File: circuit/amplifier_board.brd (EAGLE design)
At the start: 160 x 100 mm, 17 parts

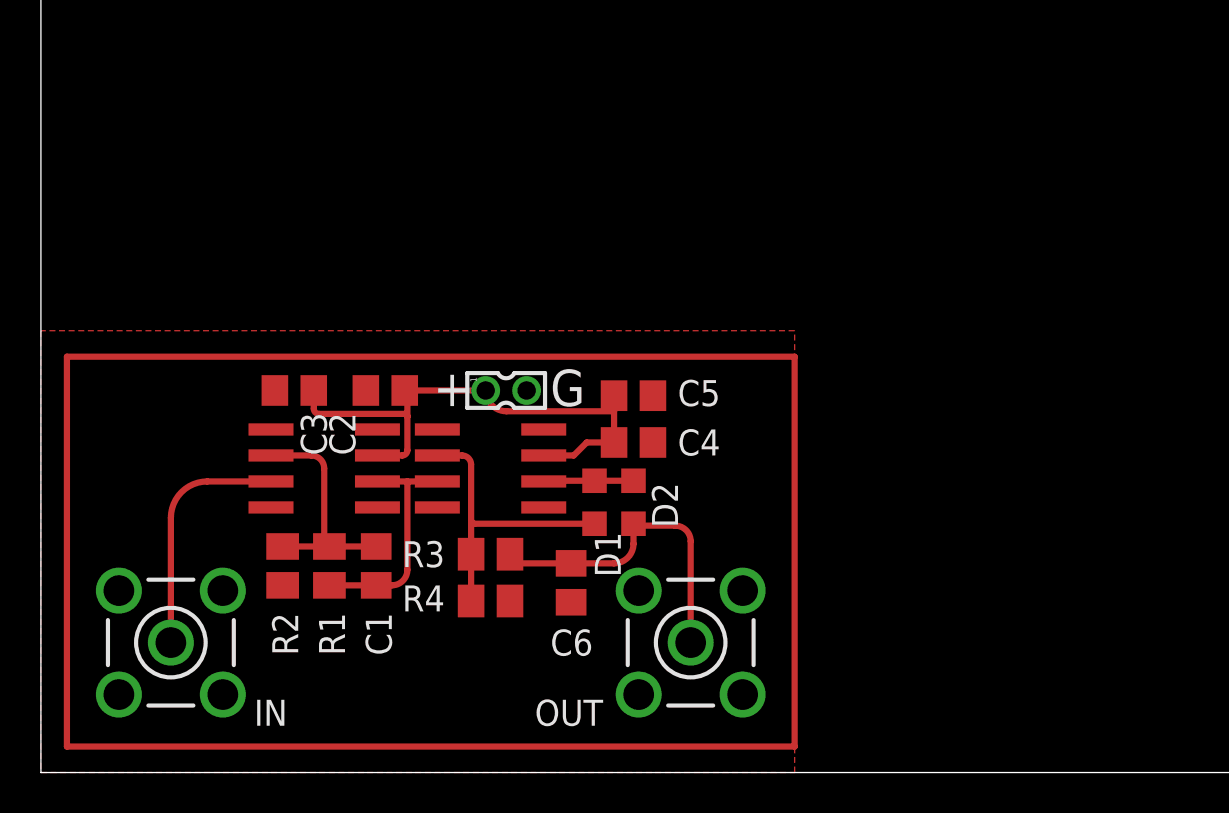
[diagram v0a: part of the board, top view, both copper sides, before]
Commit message: boards: Changed components to be correct; increased board size to be solderable.
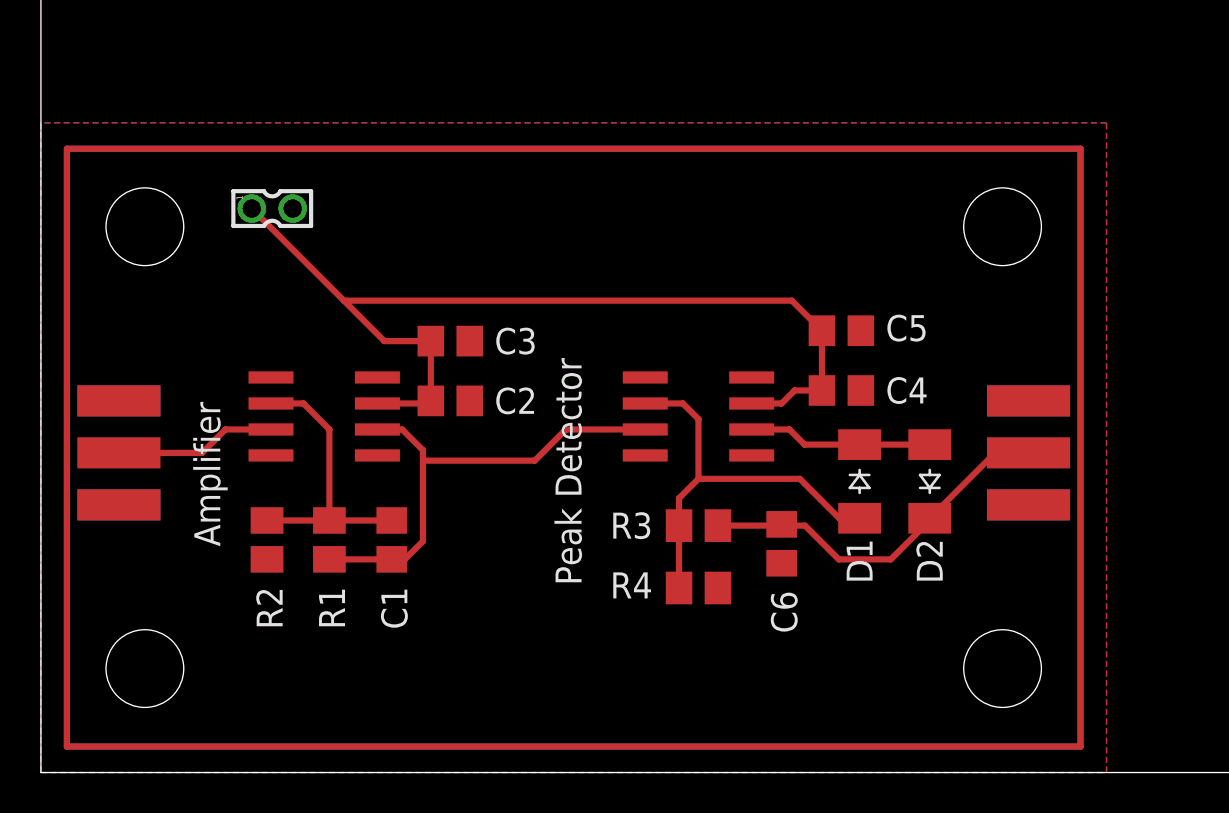
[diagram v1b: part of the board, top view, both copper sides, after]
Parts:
- C6: value 10uF -> 10nF
- D1, D2: value (none) -> MBR0540CT-ND; device 000phys605parts:SML0805 -> diode:SOD-123_MINI-SMA
- IN, OUT: value LTI-SASF54GT -> SMA_EDGE; device con-coax:LTI-SASF54GT -> SparkFun-Retired:SMA-EDGE
- MAX4104_1: value (none) -> Amplifier
- MAX4104_2: value (none) -> Peak Detector
- moved OUT 17.8 mm to (48.3, 13.1), turned to 90 degrees
- moved D2 14.5 mm to (43.4, 14.2)
- moved SUP 14.5 mm to (11.3, 27.6)
- moved D1 13.0 mm to (40.0, 14.2)
- moved C5 10.6 mm to (39.1, 21.6)
- moved C4 10.5 mm to (39.1, 18.7)
- moved MAX4104_2 10.5 mm to (32.1, 17.4)
- moved C6 10.5 mm to (36.2, 11.2)
- moved R3 10.3 mm to (32.1, 12.1)
- moved R4 10.2 mm to (32.1, 9.02)
- moved C3 7.99 mm to (20.0, 21.1), turned to 0 degrees
- moved IN 7.19 mm to (3.81, 13.1), turned to 90 degrees
- moved C2 3.22 mm to (20.0, 18.2), turned to 0 degrees
- moved MAX4104_1 2.54 mm to (13.8, 17.4)
- moved C1 1.48 mm to (17.1, 11.4)
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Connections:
- net DIG_READOUT: now also OUT.SIG; no longer OUT.1
- net GND: now also IN.GND@0, IN.GND@1, IN.GND@2, IN.GND@3, OUT.GND@0, OUT.GND@1, OUT.GND@2, OUT.GND@3; no longer IN.2, IN.3, IN.4, IN.5, OUT.2, OUT.3, OUT.4, OUT.5
- net IN: now also IN.SIG; no longer IN.1
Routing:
- net N$2: track 0.00 -> 157.5 mm
- net N$1: track 109.2 -> 157.5 mm
- net VCC: track 26.7 -> 47.6 mm
- net AMP: track 11.4 -> 23.5 mm
- net IN-_2: track 14.6 -> 20.2 mm
- net OUT_2: track 4.40 -> 9.06 mm
- net IN: track 11.7 -> 7.91 mm
- net IN-_1: track 11.2 -> 13.9 mm
- net DIG_READOUT: track 15.6 -> 18.1 mm
- added copper zone on layer 16, net GND
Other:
- board text removed: "+"
- board text removed: "G"

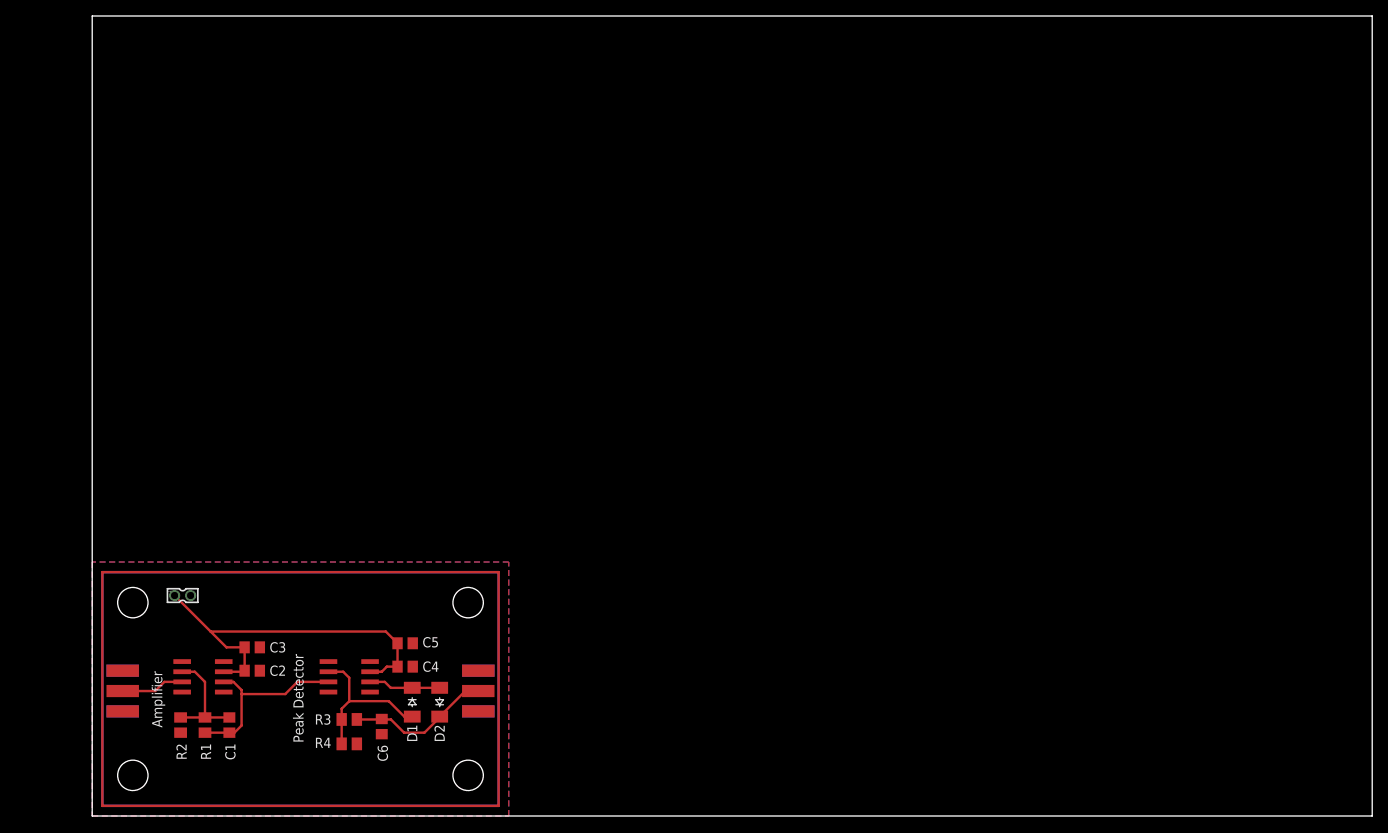
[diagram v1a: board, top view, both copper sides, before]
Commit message: boards: Increased trace clearance for easier hand soldering; reworked some traces so ground path isn't as long
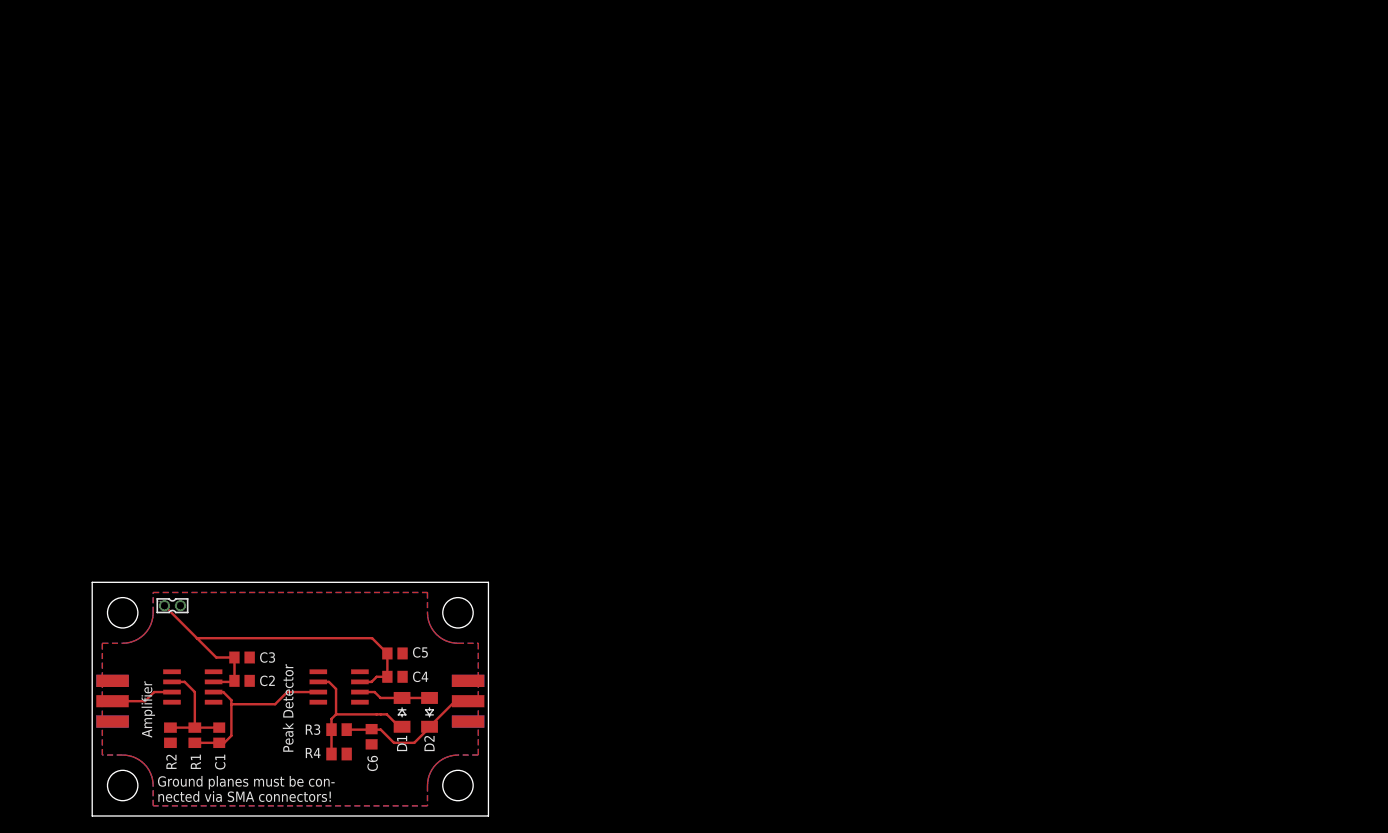
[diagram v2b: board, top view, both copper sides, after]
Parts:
- moved C2 1.80 mm to (18.7, 16.9)
- moved C4 1.80 mm to (37.8, 17.4)
- moved C5 1.80 mm to (37.8, 20.3)
- moved C6 1.80 mm to (34.9, 9.91)
- moved D1 1.80 mm to (38.7, 13.0)
- moved SUP 1.80 mm to (10.0, 26.3)
- moved IN 1.80 mm to (2.54, 11.8)
- moved C1 1.80 mm to (15.9, 10.1)
- moved C3 1.80 mm to (18.7, 19.8)
- moved MAX4104_1 1.80 mm to (12.6, 16.1)
- moved MAX4104_2 1.80 mm to (30.9, 16.1)
- moved R1 1.80 mm to (12.8, 10.1)
- moved R2 1.80 mm to (9.78, 10.1)
- moved R3 1.80 mm to (30.9, 10.8)
- moved R4 1.80 mm to (30.9, 7.75)
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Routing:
- net N$2: track 157.5 -> 0.00 mm
- net N$1: track 157.5 -> 0.00 mm
- net VCC: track 47.6 -> 48.2 mm
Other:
- board size 160 x 100 mm -> 49.5 x 29.2 mm
- board text added: "Ground planes must be con- nected via SMA connectors!"

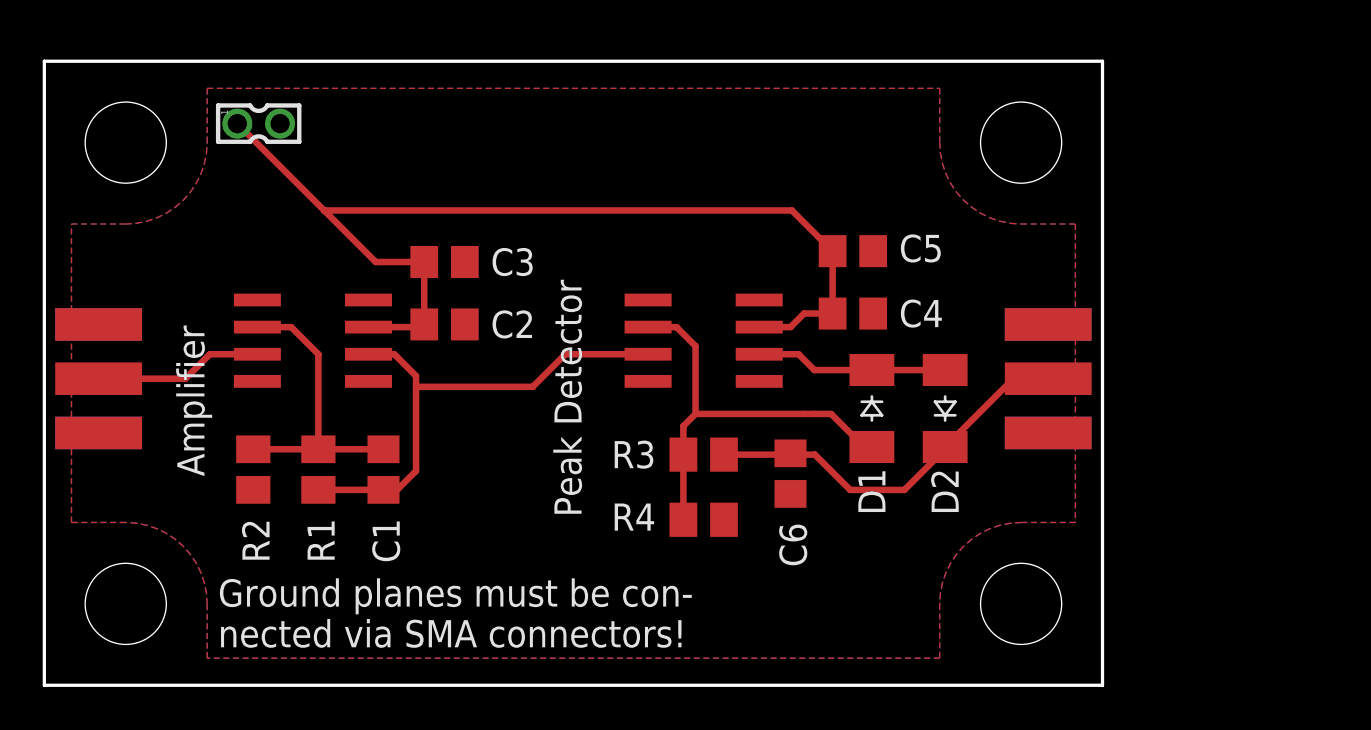
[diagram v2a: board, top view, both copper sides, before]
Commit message: boards; docs: Updated docs with impedance calculator; updated board design to stack, be solderable, and use new package design for FC-600XX.
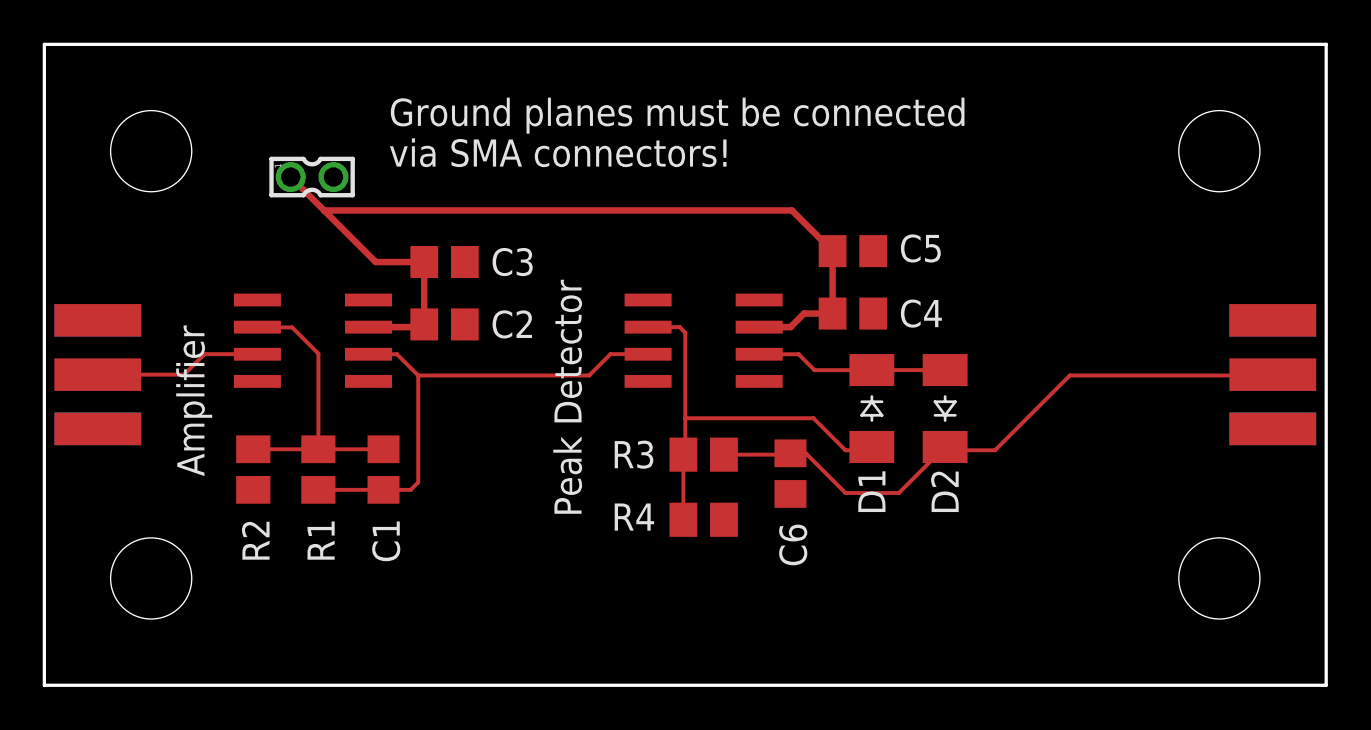
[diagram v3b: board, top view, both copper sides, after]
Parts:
- moved OUT 10.5 mm to (57.5, 12.0)
- moved SUP 3.54 mm to (12.5, 23.8)
- moved IN 0.19 mm to (2.50, 12.0)
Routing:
- net DIG_READOUT: track 18.1 -> 29.2 mm
- net VCC: track 48.2 -> 44.7 mm
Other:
- board size 49.5 x 29.2 mm -> 60 x 30 mm
- board text added: "Ground planes must be connected via SMA connectors!"
- board text removed: "Ground planes must be con- nected via SMA connectors!"

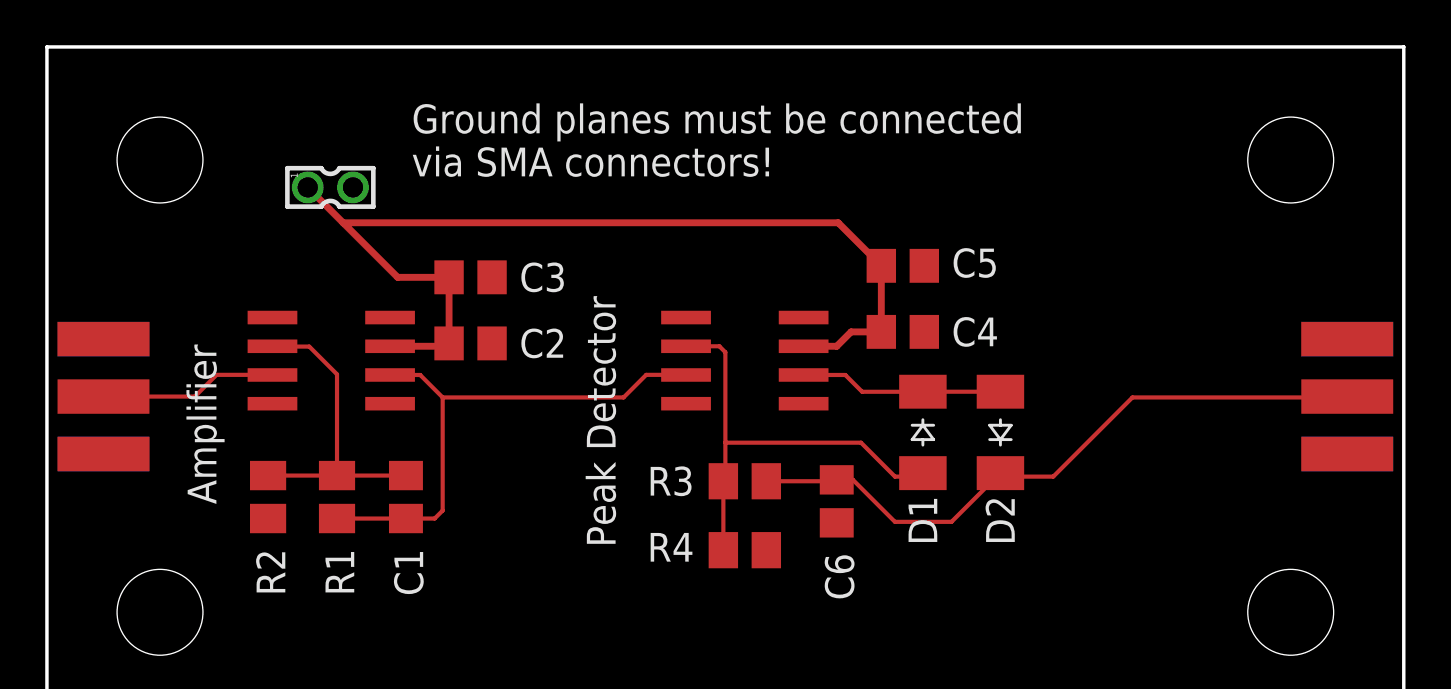
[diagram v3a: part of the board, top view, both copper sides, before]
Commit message: boards: Changes to library and board designs.
Will I need to remove the vias and replace them with holes in order to be able to ground both sides?
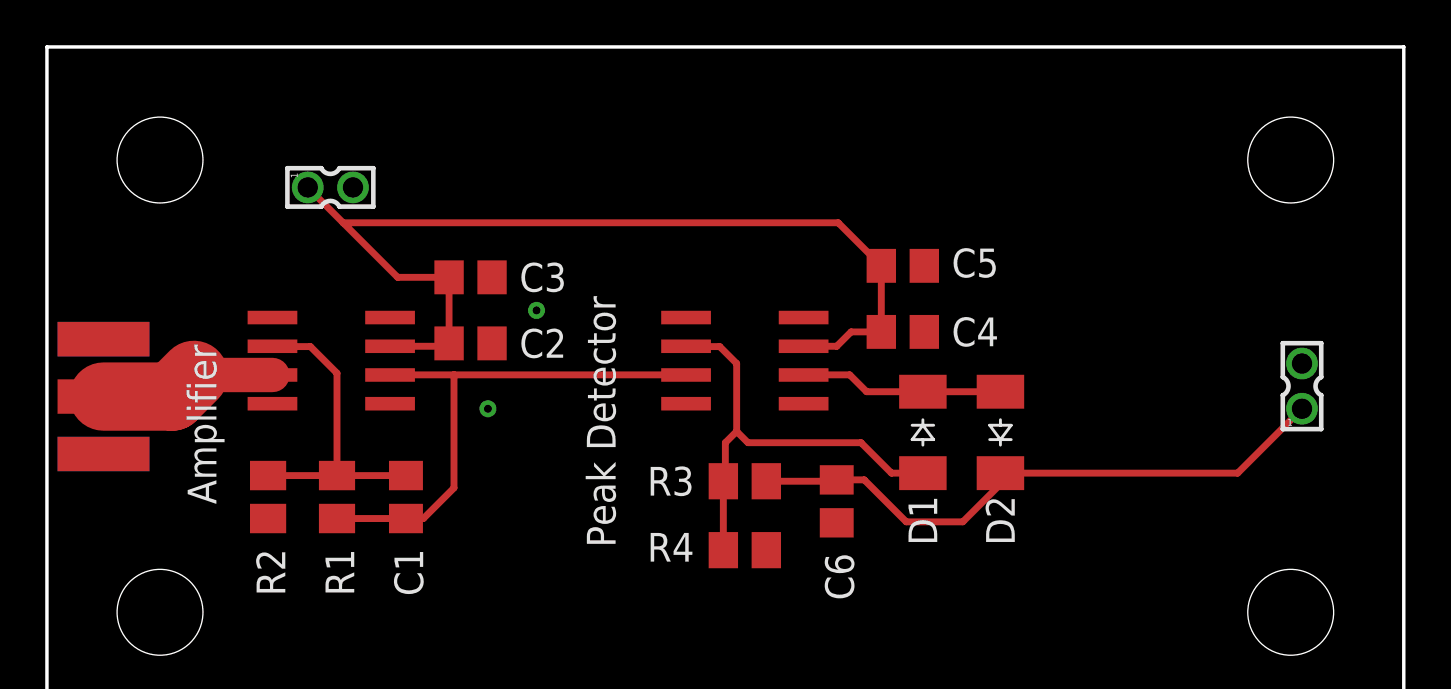
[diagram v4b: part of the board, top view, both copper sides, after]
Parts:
- removed OUT: SMA_EDGE, SparkFun-Retired:SMA-EDGE
- added SUP1: 332-02, con-garry:332-02
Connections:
- net DIG_READOUT: now also SUP1.1; no longer OUT.SIG
- net GND: now also SUP1.2; no longer OUT.GND@0, OUT.GND@1, OUT.GND@2, OUT.GND@3
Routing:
- net DIG_READOUT: track 29.2 -> 26.8 mm
- net IN-_2: track 20.1 -> 20.9 mm
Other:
- board text removed: "Ground planes must be connected via SMA connectors!"
